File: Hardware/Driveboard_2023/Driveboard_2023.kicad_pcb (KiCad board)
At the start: 2 copper layers, 122.6 x 92.7 mm, 81 parts, among them J1 6P6C, J2 RJ45_LED_Shielded, SW1 SW_Push, SW2 SW_Push, SW3 SW_Push, SW4 SW_Push, SW5 SW_Push, SW6 SW_Push, SW7 SW_SPDT, U1 Teensy4.1_DEV-16771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

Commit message: Reverse Switch Moved
Moved switch to stop it from covering traces.
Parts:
- moved SW7 6.75 mm to (205.7, 68.6)
- moved Conn1 1.20 mm to (150.2, 88.1)
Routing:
- net REVERSE_DIR: track 21.0 -> 25.8 mm
- net +3V3: track 206.9 -> 210.5 mm
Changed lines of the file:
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@@
   )
   (footprint "Button_Switch_THT:SW_Slide_1P2T_CK_OS102011MS2Q" (layer "F.Cu")
-    (at 202.9025 74.708 -90)
+    (at 205.74 68.58 -90)
     (descr "CuK miniature slide switch, OS series, SPDT, https://www.ckswitches.com/media/1428/os.pdf")
     (tags "switch SPDT")
@@
   )
   (footprint "MRDT_Connectors:Square_Anderson_2_H_Side_By_Side" (layer "F.Cu")
-    (at 150.9318 87.122)
+    (at 150.2346 88.096)
     (property "Sheetfile" "Driveboard_2023.kicad_sch")
     (property "Sheetname" "")
@@
       (effects (font (size 1 1) (thickness 0.15)))
     )
-    (fp_text value "AndersonPP" (at -17.351 -30.1) (layer "F.Fab")
+    (fp_text value "AndersonPP" (at -19.2943 -30.328) (layer "F.Fab") hide
       (effects (font (size 1 1) (thickness 0.15)))
     )
@@
     (pad "1" thru_hole oval locked (at -0.3746 0.55) (size 3 5.1) (drill oval 2 4.1) (layers *.Cu *.Mask "F.Paste")
       (net 1 "+36V") (pintype "input"))
+    (pad "2" thru_hole oval locked (at -0.3746 8.424) (size 3 5.1) (drill oval 2 4.1) (layers *.Cu *.Mask "F.Paste"))
     (pad "2" thru_hole oval locked (at -0.3746 8.424) (size 3 5.1) (drill oval 2 4.1) (layers *.Cu *.Mask "F.Paste"))
     (model "${MRDT_KICAD_LIBRARIES}/3D Files/MRDT_Connctors/Anderson_2_Horizontal_Side_by_Side.stp"
@@
     (effects (font (size 1 1) (thickness 0.15)))
   )
-  (gr_text "REVERSE" (at 208.026 76.708 90) (layer "F.SilkS")
+  (gr_text "REVERSE" (at 210.82 76.2 90) (layer "F.SilkS")
     (effects (font (size 3.048 3.048) (thickness 0.15)))
   )
@@
   (segment (start 163.741 87.672) (end 154.644 87.672) (width 0.25) (layer "F.Cu") (net 1))
   (segment (start 154.644 87.672) (end 150.5572 87.672) (width 0.25) (layer "F.Cu") (net 1))
+  (segment (start 208.28 68.58) (end 205.74 68.58) (width 0.25) (layer "F.Cu") (net 3))
   (segment (start 242.594 65.488) (end 242.594 72.688) (width 0.25) (layer "F.Cu") (net 3))
   (segment (start 240.8095 63.7035) (end 216.19 63.7035) (width 0.25) (layer "F.Cu") (net 3))
+  (segment (start 214.1975 72.896) (end 212.596 72.896) (width 0.25) (layer "F.Cu") (net 3))
+  (segment (start 212.596 72.896) (end 208.28 68.58) (width 0.25) (layer "F.Cu") (net 3))
   (segment (start 214.23675 86.89475) (end 214.23675 79.69475) (width 0.25) (layer "F.Cu") (net 3))
   (segment (start 242.57 86.89475) (end 242.57 79.69475) (width 0.25) (layer "F.Cu") (net 3))
@@
   (segment (start 169.7755 85.852) (end 166.9815 83.058) (width 0.25) (layer "F.Cu") (net 3))
   (segment (start 214.23675 79.69475) (end 214.23675 72.93525) (width 0.25) (layer "F.Cu") (net 3))
-  (segment (start 212.3855 74.708) (end 202.9025 74.708) (width 0.25) (layer "F.Cu") (net 3))
   (segment (start 242.57 79.69475) (end 242.57 72.712) (width 0.25) (layer "F.Cu") (net 3))
   (segment (start 242.57 72.712) (end 242.594 72.688) (width 0.25) (layer "F.Cu") (net 3))
@@
   (segment (start 170.434 85.1935) (end 169.7755 85.852) (width 0.25) (layer "F.Cu") (net 3))
   (segment (start 161.6445 83.058) (end 161.036 83.6665) (width 0.25) (layer "F.Cu") (net 3))
-  (segment (start 214.1975 72.896) (end 212.3855 74.708) (width 0.25) (layer "F.Cu") (net 3))
   (segment (start 216.19 63.7035) (end 216.13525 63.75825) (width 0.25) (layer "F.Cu") (net 3))
   (segment (start 170.434 74.168) (end 171.196 73.406) (width 0.25) (layer "F.Cu") (net 3))
@@
   (via (at 171.196 73.406) (size 0.8) (drill 0.4) (layers "F.Cu" "B.Cu") (net 3))
   (segment (start 142.24 73.406) (end 171.196 73.406) (width 0.25) (layer "B.Cu") (net 3))
+  (segment (start 197.072 74.708) (end 181.896 74.708) (width 0.25) (layer "B.Cu") (net 3))
+  (segment (start 181.896 74.708) (end 180.594 73.406) (width 0.25) (layer "B.Cu") (net 3))
   (segment (start 139.954 63.246) (end 139.954 71.12) (width 0.25) (layer "B.Cu") (net 3))
-  (segment (start 181.896 74.708) (end 180.594 73.406) (width 0.25) (layer "B.Cu") (net 3))
-  (segment (start 202.9025 74.708) (end 181.896 74.708) (width 0.25) (layer "B.Cu") (net 3))
+  (segment (start 205.74 68.58) (end 203.2 68.58) (width 0.25) (layer "B.Cu") (net 3))
+  (segment (start 203.2 68.58) (end 197.072 74.708) (width 0.25) (layer "B.Cu") (net 3))
   (segment (start 139.954 71.12) (end 142.24 73.406) (width 0.25) (layer "B.Cu") (net 3))
   (segment (start 171.196 73.406) (end 180.594 73.406) (width 0.25) (layer "B.Cu") (net 3))
@@
   (segment (start 174.752 80.264) (end 172.974 78.486) (width 0.25) (layer "B.Cu") (net 40))
   (segment (start 244.602 76.708) (end 210.82 76.708) (width 0.25) (layer "B.Cu") (net 40))
-  (segment (start 202.9025 76.708) (end 198.4925 76.708) (width 0.25) (layer "F.Cu") (net 41))
+  (segment (start 205.74 70.58) (end 203.4425 70.58) (width 0.25) (layer "F.Cu") (net 41))
   (segment (start 196.2235 76.0815) (end 193.294 73.152) (width 0.25) (layer "F.Cu") (net 41))
-  (segment (start 198.4925 76.708) (end 197.866 76.0815) (width 0.25) (layer "F.Cu") (net 41))
+  (segment (start 203.4425 70.58) (end 197.941 76.0815) (width 0.25) (layer "F.Cu") (net 41))
   (segment (start 193.294 73.152) (end 193.294 63.246) (width 0.25) (layer "F.Cu") (net 41))
+  (segment (start 197.941 76.0815) (end 197.866 76.0815) (width 0.25) (layer "F.Cu") (net 41))
   (segment (start 197.866 76.0815) (end 196.2235 76.0815) (width 0.25) (layer "F.Cu") (net 41))
   (segment (start 163.83 45.212) (end 163.83 50.179) (width 0.25) (layer "F.Cu") (net 58))

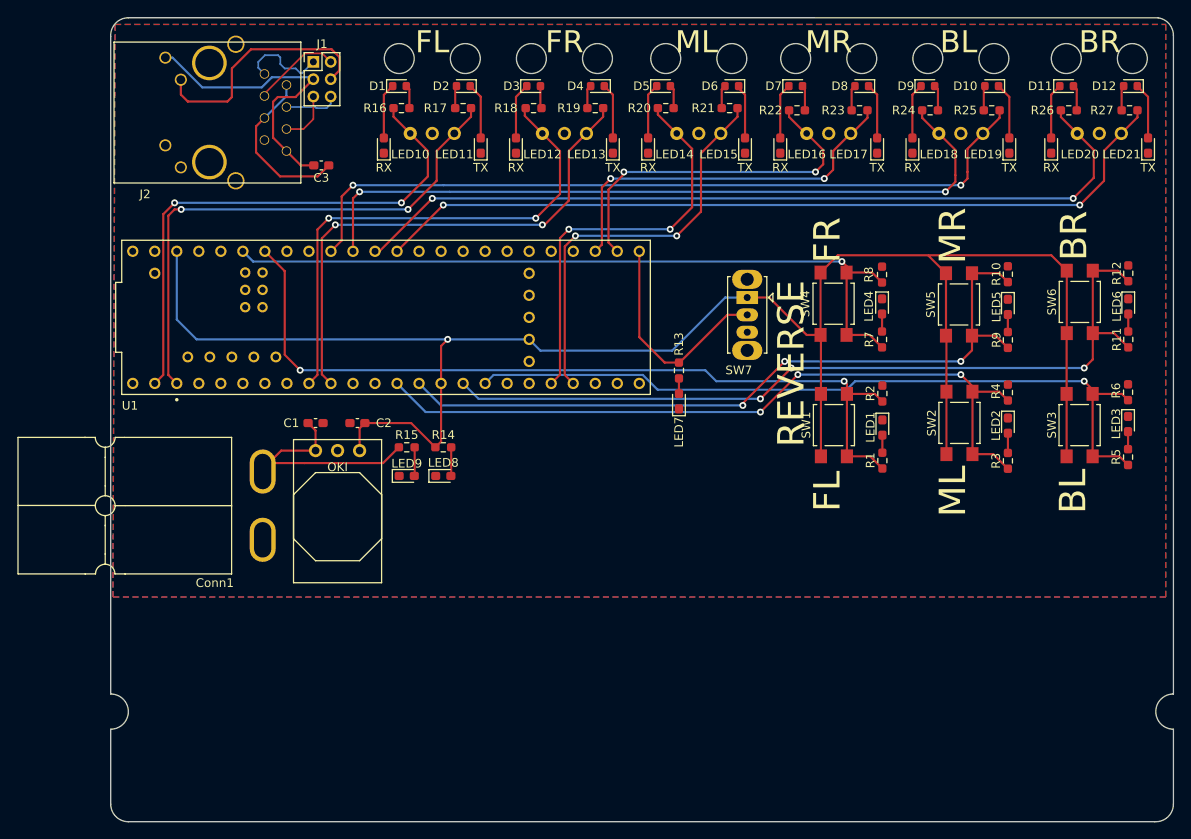
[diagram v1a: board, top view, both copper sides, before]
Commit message: Layout Review Board
Finished Changes. Needs to add signatures.
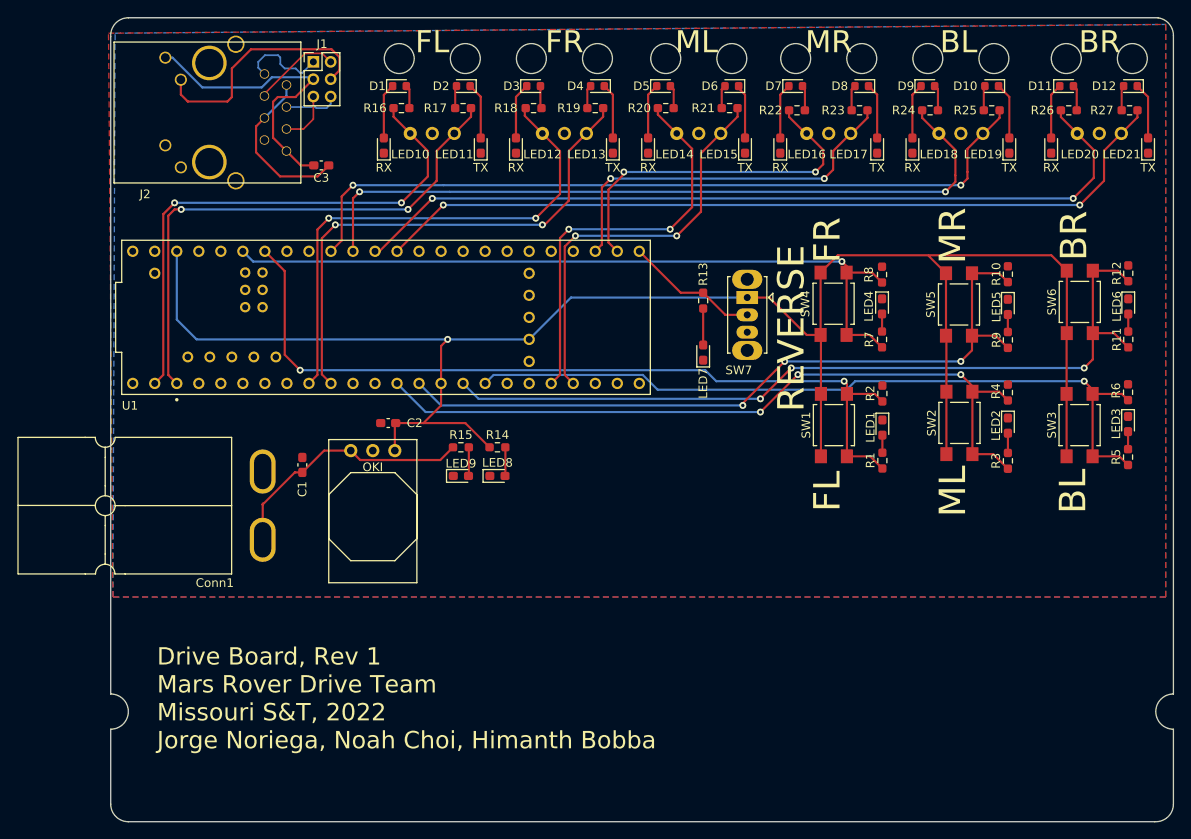
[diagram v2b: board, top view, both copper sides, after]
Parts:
- moved R13 8.53 mm to (200.7, 68.9)
- moved LED7 6.28 mm to (200.7, 74.9)
- moved LED8 6.25 mm to (176.9, 89.2)
- moved R14 6.25 mm to (176.9, 85.9)
- moved LED9 6.25 mm to (172.7, 89.2)
- moved R15 6.25 mm to (172.7, 85.9)
- moved C1 5.06 mm to (154.4, 87.9), turned to 90 degrees
- moved U2 4.06 mm to (160.0, 86.2)
- moved C2 3.56 mm to (164.3, 83.1)
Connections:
- Conn1 pad 1: +36V -> GND
- Conn1 pad 2: (no net) -> +36V
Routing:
- net REVERSE_DIR: track 25.8 -> 15.5 mm
- net +36V: track 25.3 -> 29.8 mm
- net Net-(LED7-Pad2): track 1.77 -> 4.21 mm
- net +3V3: track 210.5 -> 209.7 mm
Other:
- board text added: "Drive Board, Rev 1 Mars Rover Drive Team Missouri S&T, 2022 Jorge Noriega, Noah Choi, Himanth Bobba"
